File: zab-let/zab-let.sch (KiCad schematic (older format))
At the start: 37 parts, among them J1 CONN_3, J2 CONN_4X2, Q1 BC547, Q2 BC547, Q3 BC547, Q4 BC547, Q5 BC557, SW1 SW_PUSH, U1 ATTINY24-44-84/DIP-SO, X1 8MHz

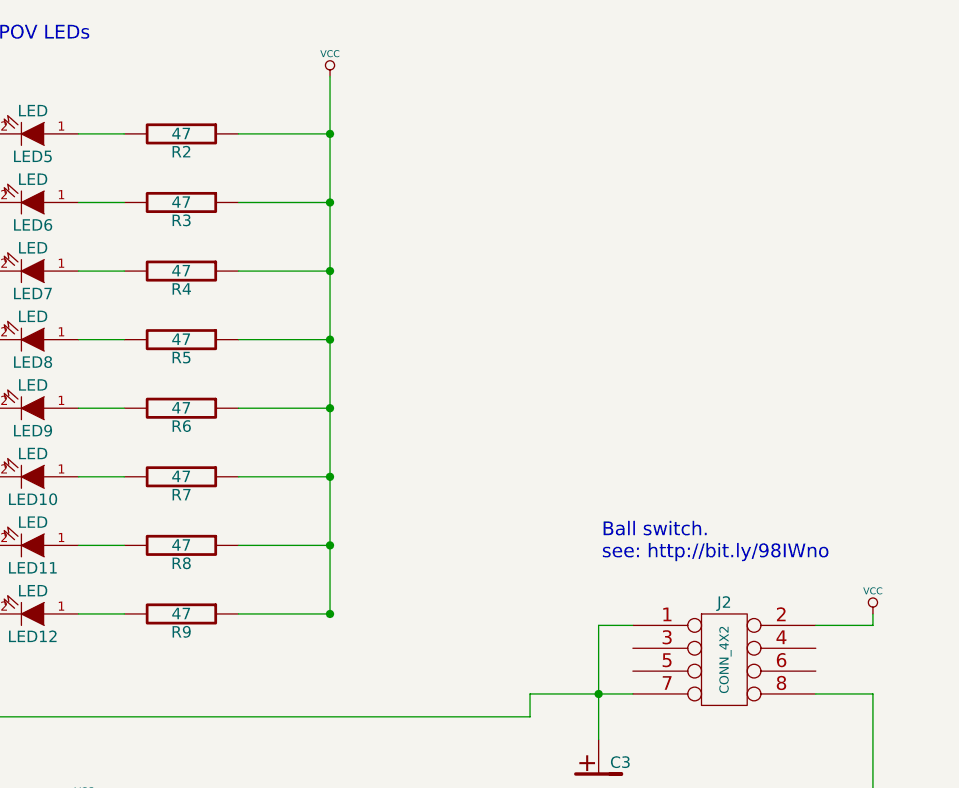
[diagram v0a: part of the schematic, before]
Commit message: så er der også pillet ved modstandende til LED'erne, de er nu 125 ohm
git-svn-id: file:///home/ff/projects/osaa/svn@209 a092026d-3e22-4cff-94a7-eaa6fdd35d37
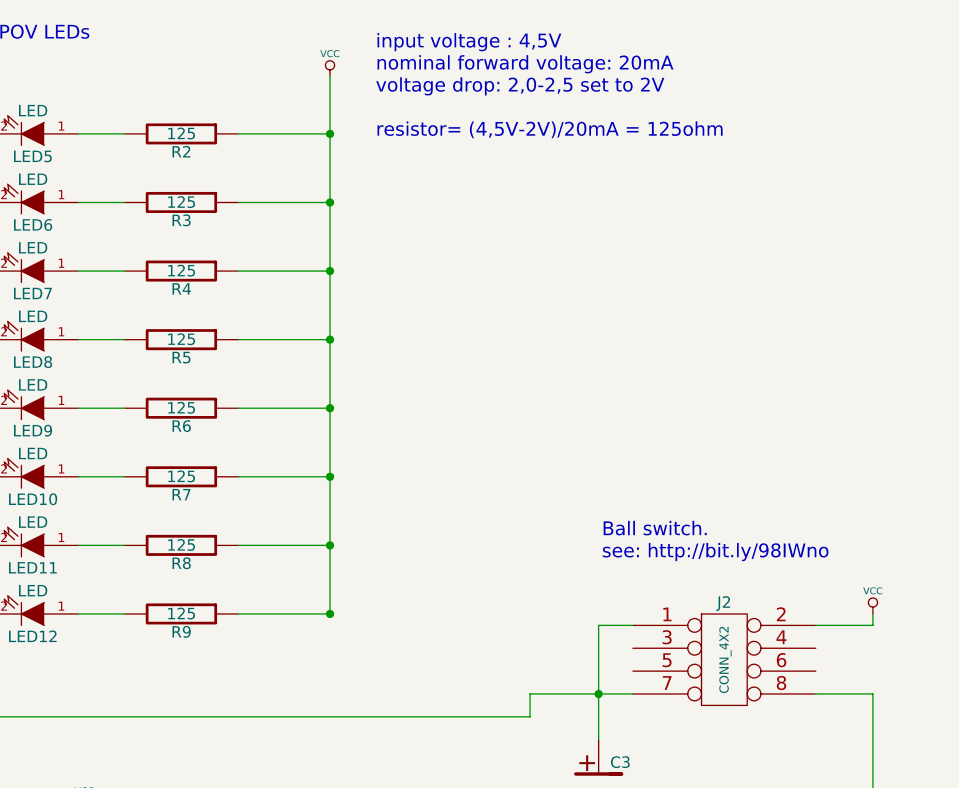
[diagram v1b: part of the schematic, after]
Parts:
- R2, R3, R4, R5, R6, R7, R8, R9: value 47 -> 125
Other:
- note added: "input voltage : 4,5V\nnominal forward voltage: 20mA\nvoltage drop: 2,0-2,5 set to 2V\n\nresistor= (4,5V-2V)/20mA = 125ohm"
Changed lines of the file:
@@
-EESchema Schematic File Version 2  date 08-11-2010 17:45:19
+EESchema Schematic File Version 2  date 13-12-2010 11:04:57
 LIBS:power
 LIBS:device
@@
 LIBS:attiny
 LIBS:atmel_2
-LIBS:TV-begone_POV-cache
+LIBS:zab-let-cache
 EELAYER 24  0
 EELAYER END
@@
 Sheet 1 1
 Title ""
-Date "8 nov 2010"
+Date "13 dec 2010"
 Rev ""
 Comp ""
@@
 Comment4 ""
 $EndDescr
+Text Notes 7650 1100 0    60   ~ 0
+input voltage : 4,5V\nnominal forward voltage: 20mA\nvoltage drop: 2,0-2,5 set to 2V\n\nresistor= (4,5V-2V)/20mA = 125ohm
 Wire Wire Line
 	2550 950  2550 850
@@
 P 6800 3175
 F 0 "R9" V 6880 3175 50  0000 C CNN
-F 1 "47" V 6800 3175 50  0000 C CNN
+F 1 "125" V 6800 3175 50  0000 C CNN
 	1    6800 3175
 	0    1    1    0
@@
 P 6800 2875
 F 0 "R8" V 6880 2875 50  0000 C CNN
-F 1 "47" V 6800 2875 50  0000 C CNN
+F 1 "125" V 6800 2875 50  0000 C CNN
 	1    6800 2875
 	0    1    1    0
@@
 P 6800 1075
 F 0 "R2" V 6880 1075 50  0000 C CNN
-F 1 "47" V 6800 1075 50  0000 C CNN
+F 1 "125" V 6800 1075 50  0000 C CNN
 	1    6800 1075
 	0    1    1    0
@@
 P 6800 1375
 F 0 "R3" V 6880 1375 50  0000 C CNN
-F 1 "47" V 6800 1375 50  0000 C CNN
+F 1 "125" V 6800 1375 50  0000 C CNN
 	1    6800 1375
 	0    1    1    0
@@
 P 6800 1675
 F 0 "R4" V 6880 1675 50  0000 C CNN
-F 1 "47" V 6800 1675 50  0000 C CNN
+F 1 "125" V 6800 1675 50  0000 C CNN
 	1    6800 1675
 	0    1    1    0
@@
 P 6800 1975
 F 0 "R5" V 6880 1975 50  0000 C CNN
-F 1 "47" V 6800 1975 50  0000 C CNN
+F 1 "125" V 6800 1975 50  0000 C CNN
 	1    6800 1975
 	0    1    1    0
@@
 P 6800 2575
 F 0 "R7" V 6880 2575 50  0000 C CNN
-F 1 "47" V 6800 2575 50  0000 C CNN
+F 1 "125" V 6800 2575 50  0000 C CNN
 	1    6800 2575
 	0    1    1    0
@@
 P 6800 2275
 F 0 "R6" V 6880 2275 50  0000 C CNN
-F 1 "47" V 6800 2275 50  0000 C CNN
+F 1 "125" V 6800 2275 50  0000 C CNN
 	1    6800 2275
 	0    1    1    0

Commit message: added missing libraries
git-svn-id: file:///home/ff/projects/osaa/svn@244 a092026d-3e22-4cff-94a7-eaa6fdd35d37
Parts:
- U1: footprint DIL-14 -> (none); Elfa: 73-219-24 -> (none)
- X1: value 8MHz -> RESONATOR; Elfa: 74-702-06 -> (none)
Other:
- moved on the sheet: BT1, C1, C2, C3, J1, J2, LED1, LED10, LED11, LED12, LED2, LED3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
